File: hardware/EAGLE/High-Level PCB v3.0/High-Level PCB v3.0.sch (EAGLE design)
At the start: 57 parts, among them IC1 MCP2551, IC2 DS8921, IC3 DS8921, J1 Optical Mouse, J2 RaspπUart, J3 Gyro, J4 Micro-SD, J7 ODO_JACK, J8 DB9 Plug, J9 CAN Output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

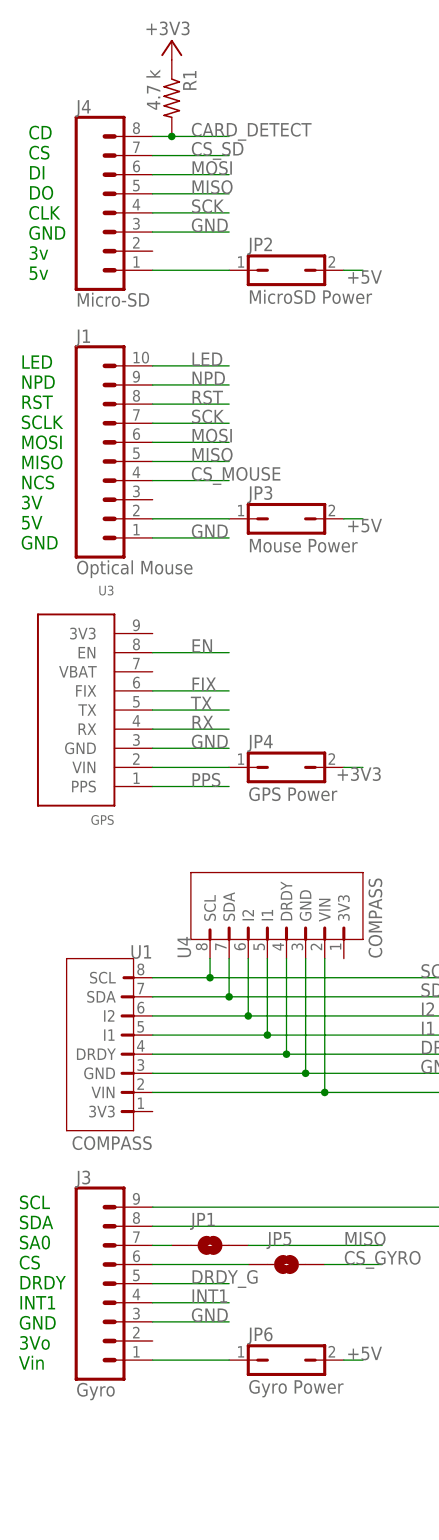
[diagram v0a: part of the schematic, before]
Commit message: added footprints
Includes footprints for all breakout boards except optical mouse
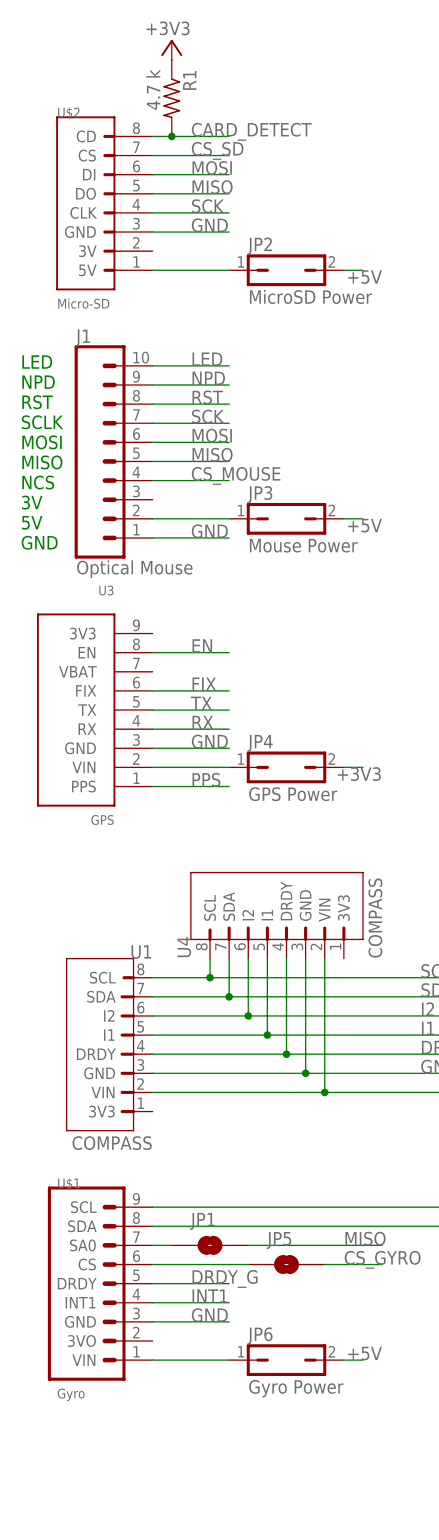
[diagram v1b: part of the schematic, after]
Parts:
- removed J3: Gyro, SparkFun-Connectors:CONN_09
- removed J4: Micro-SD, SparkFun-Connectors:CONN_08"
- added U$1: Gyro, ELCano_Footprints:ELGYRO_L3GD20H
- added U$2: Micro-SD, ELCano_Footprints:MINI_SD
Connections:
- net CARD_DETECT: now also U$2.CD; no longer J4.8
- net CS_SD: now also U$2.CS; no longer J4.7
- net DRDY_G: now also U$1.DRDY; no longer J3.5
- net GND: now also U$1.GND, U$2.GND; no longer J3.3, J4.3
- net INT1: now also U$1.INT1; no longer J3.4
- net MISO: now also U$2.DO; no longer J4.5
- net MOSI: now also U$2.DI; no longer J4.6
- net N$10: now also U$2.5V; no longer J4.1
- net N$19: now also U$1.CS; no longer J3.6
- net N$20: now also U$1.SA0; no longer J3.7
- net N$21: now also U$1.SDA; no longer J3.8
- net N$22: now also U$1.SCL; no longer J3.9
- net N$9: now also U$1.VIN; no longer J3.1
- net SCK: now also U$2.CLK; no longer J4.4
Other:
- note removed: "CD CS DI DO CLK GND 3v 5v"
- note removed: "SCL SDA SA0 CS DRDY INT1 GND 3Vo Vin"
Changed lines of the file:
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@@
 <part name="+3V31" library="supply1" library_urn="urn:adsk.eagle:library:371" deviceset="+3V3" device=""/>
 <part name="JP7" library="jumper" library_urn="urn:adsk.eagle:library:252" deviceset="JP1Q" device="" package3d_urn="urn:adsk.eagle:package:15455/1" value="Compass Power"/>
-<part name="J3" library="SparkFun-Connectors" library_urn="urn:adsk.eagle:library:513" deviceset="CONN_09" device="" package3d_urn="urn:adsk.eagle:package:38153/1" value="Gyro"/>
 <part name="JP6" library="jumper" library_urn="urn:adsk.eagle:library:252" deviceset="JP1Q" device="" package3d_urn="urn:adsk.eagle:package:15455/1" value="Gyro Power"/>
 <part name="JP1" library="SparkFun-Jumpers" deviceset="JUMPER-SMT_2_NO" device="_SILK" value=""/>
@@
 <part name="JP9" library="SparkFun-Jumpers" deviceset="JUMPER-SMT_3_1-NC_TRACE" device="_SILK" value=""/>
 <part name="GND5" library="SparkFun-PowerSymbols" deviceset="GND" device=""/>
-<part name="J4" library="SparkFun-Connectors" library_urn="urn:adsk.eagle:library:513" deviceset="CONN_08" device="&quot;" package3d_urn="urn:adsk.eagle:package:38138/1" value="Micro-SD"/>
 <part name="J1" library="SparkFun-Connectors" library_urn="urn:adsk.eagle:library:513" deviceset="CONN_10" device="&quot;" package3d_urn="urn:adsk.eagle:package:38157/1" value="Optical Mouse"/>
 <part name="TP1" library="testpad" library_urn="urn:adsk.eagle:library:385" deviceset="TP" device="PAD1-17" package3d_urn="urn:adsk.eagle:package:27949/1"/>
@@
 <part name="J2" library="tx_rxRasp" deviceset="CONN_02" device="" value="RaspπUart"/>
 <part name="GND14" library="SparkFun-PowerSymbols" deviceset="GND" device=""/>
+<part name="U$1" library="ELCano_Footprints" deviceset="ELGYRO_L3GD20H" device="" value="Gyro"/>
+<part name="U$2" library="ELCano_Footprints" deviceset="MINI_SD" device="" value="Micro-SD"/>
 </parts>
 <sheets>
@@
 5V
 GND</text>
-<text x="16.51" y="214.63" size="1.778" layer="91">CD
-CS
-DI
-DO
-CLK
-GND
-3v
-5v</text>
-<text x="15.24" y="69.85" size="1.778" layer="91">SCL
-SDA
-SA0
-CS
-DRDY
-INT1
-GND
-3Vo
-Vin</text>
 <text x="292.1" y="7.62" size="3.81" layer="97">The Elcano Project</text>
 </plain>
@@
 </instance>
 <instance part="JP7" gate="A" x="81.28" y="106.68" rot="R270"/>
-<instance part="J3" gate="G$1" x="22.86" y="81.28"/>
 <instance part="JP6" gate="A" x="50.8" y="71.12" rot="R270"/>
 <instance part="JP1" gate="G$1" x="40.64" y="86.36"/>
@@
 <instance part="JP9" gate="G$1" x="81.28" y="76.2" rot="MR180"/>
 <instance part="GND5" gate="1" x="175.26" y="33.02"/>
-<instance part="J4" gate="G$1" x="27.94" y="223.52"/>
 <instance part="J1" gate="G$1" x="22.86" y="198.12"/>
 <instance part="TP1" gate="G$1" x="360.68" y="76.2" smashed="yes" rot="R90">
@@
 <instance part="J2" gate="G$1" x="261.62" y="121.92" rot="MR0"/>
 <instance part="GND14" gate="1" x="254" y="114.3"/>
+<instance part="U$1" gate="G$1" x="20.32" y="68.58"/>
+<instance part="U$2" gate="G$1" x="20.32" y="213.36"/>
 </instances>
 <busses>
@@
 <wire x1="33.02" y1="231.14" x2="43.18" y2="231.14" width="0.1524" layer="91"/>
 <label x="38.1" y="231.14" size="1.778" layer="95"/>
-<pinref part="J4" gate="G$1" pin="7"/>
+<pinref part="U$2" gate="G$1" pin="CS"/>
 </segment>
 <segment>
@@
 <wire x1="33.02" y1="220.98" x2="43.18" y2="220.98" width="0.1524" layer="91"/>
 <label x="38.1" y="220.98" size="1.778" layer="95"/>
-<pinref part="J4" gate="G$1" pin="3"/>
-</segment>
-<segment>
-<pinref part="J3" gate="G$1" pin="3"/>
+<pinref part="U$2" gate="G$1" pin="GND"/>
+</segment>
+<segment>
 <wire x1="33.02" y1="76.2" x2="43.18" y2="76.2" width="0.1524" layer="91"/>
 <label x="38.1" y="76.2" size="1.778" layer="95"/>
+<pinref part="U$1" gate="G$1" pin="GND"/>
 </segment>
 <segment>
@@
 <net name="INT1" class="0">
 <segment>
-<pinref part="J3" gate="G$1" pin="4"/>
 <wire x1="33.02" y1="78.74" x2="43.18" y2="78.74" width="0.1524" layer="91"/>
 <label x="38.1" y="78.74" size="1.778" layer="95"/>
+<pinref part="U$1" gate="G$1" pin="INT1"/>
 </segment>
 <segment>
@@
 <net name="DRDY_G" class="0">
 <segment>
-<pinref part="J3" gate="G$1" pin="5"/>
 <wire x1="33.02" y1="81.28" x2="43.18" y2="81.28" width="0.1524" layer="91"/>
 <label x="38.1" y="81.28" size="1.778" layer="95"/>
+<pinref part="U$1" gate="G$1" pin="DRDY"/>
 </segment>
 <segment>
@@
 <wire x1="33.02" y1="223.52" x2="43.18" y2="223.52" width="0.1524" layer="91"/>
 <label x="38.1" y="223.52" size="1.778" layer="95"/>
-<pinref part="J4" gate="G$1" pin="4"/>
+<pinref part="U$2" gate="G$1" pin="CLK"/>
 </segment>
 <segment>
@@
 <wire x1="33.02" y1="228.6" x2="43.18" y2="228.6" width="0.1524" layer="91"/>
 <label x="38.1" y="228.6" size="1.778" layer="95"/>
-<pinref part="J4" gate="G$1" pin="6"/>
+<pinref part="U$2" gate="G$1" pin="DI"/>
 </segment>
 <segment>
@@
 <wire x1="33.02" y1="226.06" x2="43.18" y2="226.06" width="0.1524" layer="91"/>
 <label x="38.1" y="226.06" size="1.778" layer="95"/>
-<pinref part="J4" gate="G$1" pin="5"/>
+<pinref part="U$2" gate="G$1" pin="DO"/>
 </segment>
 <segment>
@@
 <segment>
 <wire x1="43.18" y1="71.12" x2="33.02" y2="71.12" width="0.1524" layer="91"/>
-<pinref part="J3" gate="G$1" pin="1"/>
 <pinref part="JP6" gate="A" pin="1"/>
+<pinref part="U$1" gate="G$1" pin="VIN"/>
 </segment>
 </net>
@@
 <pinref part="JP2" gate="A" pin="1"/>
 <wire x1="33.02" y1="215.9" x2="43.18" y2="215.9" width="0.1524" layer="91"/>
-<pinref part="J4" gate="G$1" pin="1"/>
+<pinref part="U$2" gate="G$1" pin="5V"/>
 </segment>
 </net>
@@
 <junction x="35.56" y="233.68"/>
 <label x="38.1" y="233.68" size="1.778" layer="95"/>
-<pinref part="J4" gate="G$1" pin="8"/>
+<pinref part="U$2" gate="G$1" pin="CD"/>
 </segment>
 <segment>
@@
 <net name="N$19" class="0">
 <segment>
-<pinref part="J3" gate="G$1" pin="6"/>
 <pinref part="JP5" gate="G$1" pin="1"/>
 <wire x1="33.02" y1="83.82" x2="45.72" y2="83.82" width="0.1524" layer="91"/>
+<pinref part="U$1" gate="G$1" pin="CS"/>
 </segment>
 </net>
 <net name="N$20" class="0">
 <segment>
-<pinref part="J3" gate="G$1" pin="7"/>
 <pinref part="JP1" gate="G$1" pin="1"/>
 <wire x1="33.02" y1="86.36" x2="35.56" y2="86.36" width="0.1524" layer="91"/>
+<pinref part="U$1" gate="G$1" pin="SA0"/>
 </segment>
 </net>
 <net name="N$22" class="0">
 <segment>
-<pinref part="J3" gate="G$1" pin="9"/>
 <wire x1="33.02" y1="91.44" x2="76.2" y2="91.44" width="0.1524" layer="91"/>
 <pinref part="JP8" gate="G$1" pin="2"/>
+<pinref part="U$1" gate="G$1" pin="SCL"/>
 </segment>
 </net>
 <net name="N$21" class="0">
 <segment>
-<pinref part="J3" gate="G$1" pin="8"/>
 <wire x1="33.02" y1="88.9" x2="73.66" y2="88.9" width="0.1524" layer="91"/>
 <wire x1="73.66" y1="88.9" x2="73.66" y2="76.2" width="0.1524" layer="91"/>
 <wire x1="73.66" y1="76.2" x2="76.2" y2="76.2" width="0.1524" layer="91"/>
 <pinref part="JP9" gate="G$1" pin="2"/>
-</segment>
-</net>
+<pinref part="U$1" gate="G$1" pin="SDA"/>
+</segment>
+</net>

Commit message: Used larger resistor footprints
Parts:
- R1, R4, R5, R6: device resistor:R-US_0204/5 -> resistor:R-US_0204/7
- R2, R3, R7, R8: device rcl:R-US_0204/5 -> rcl:R-US_0204/7
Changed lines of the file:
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@@
 <part name="J7" library="elcanoParts" deviceset="ODO_JACK" device=""/>
 <part name="C2" library="capacitor-wima" library_urn="urn:adsk.eagle:library:116" deviceset="C" device="2.5/5" package3d_urn="urn:adsk.eagle:package:5407/1" value="1 uF"/>
-<part name="R4" library="resistor" library_urn="urn:adsk.eagle:library:348" deviceset="R-US_" device="0204/5" package3d_urn="urn:adsk.eagle:package:25955/1" value="4.7 k"/>
+<part name="R4" library="resistor" library_urn="urn:adsk.eagle:library:348" deviceset="R-US_" device="0204/7" package3d_urn="urn:adsk.eagle:package:25945/1" value="4.7 k"/>
 <part name="GND3" library="SparkFun-PowerSymbols" deviceset="GND" device=""/>
 <part name="X1" library="con-subd" library_urn="urn:adsk.eagle:library:189" deviceset="M25" device="H" package3d_urn="urn:adsk.eagle:package:10312/1" value="Vehicle control"/>
@@
 <part name="S2" library="elcanoParts" deviceset="DPDT_DEV" device="6X5MM_PAC" value="SPI Direction"/>
 <part name="X2" library="con-kycon" library_urn="urn:adsk.eagle:library:157" deviceset="GLX-S-88M" device="" package3d_urn="urn:adsk.eagle:package:7680/1" value="RJ45"/>
-<part name="R7" library="rcl" library_urn="urn:adsk.eagle:library:334" deviceset="R-US_" device="0204/5" package3d_urn="urn:adsk.eagle:package:23488/1" value="100"/>
+<part name="R7" library="rcl" library_urn="urn:adsk.eagle:library:334" deviceset="R-US_" device="0204/7" package3d_urn="urn:adsk.eagle:package:23498/1" value="100"/>
 <part name="X3" library="con-kycon" library_urn="urn:adsk.eagle:library:157" deviceset="GLX-S-88M" device="" package3d_urn="urn:adsk.eagle:package:7680/1" value="RJ45"/>
-<part name="R8" library="rcl" library_urn="urn:adsk.eagle:library:334" deviceset="R-US_" device="0204/5" package3d_urn="urn:adsk.eagle:package:23488/1" value="100"/>
+<part name="R8" library="rcl" library_urn="urn:adsk.eagle:library:334" deviceset="R-US_" device="0204/7" package3d_urn="urn:adsk.eagle:package:23498/1" value="100"/>
 <part name="C3" library="capacitor-wima" library_urn="urn:adsk.eagle:library:116" deviceset="C" device="2.5/5" package3d_urn="urn:adsk.eagle:package:5407/1" value="0.1 uF"/>
 <part name="C4" library="capacitor-wima" library_urn="urn:adsk.eagle:library:116" deviceset="C" device="2.5/5" package3d_urn="urn:adsk.eagle:package:5407/1" value="0.1 uF"/>
@@
 <part name="JP3" library="jumper" library_urn="urn:adsk.eagle:library:252" deviceset="JP1Q" device="" package3d_urn="urn:adsk.eagle:package:15455/1" value="Mouse Power"/>
 <part name="JP4" library="jumper" library_urn="urn:adsk.eagle:library:252" deviceset="JP1Q" device="" package3d_urn="urn:adsk.eagle:package:15455/1" value="GPS Power"/>
-<part name="R6" library="resistor" library_urn="urn:adsk.eagle:library:348" deviceset="R-US_" device="0204/5" package3d_urn="urn:adsk.eagle:package:25955/1" value="4.7 k"/>
-<part name="R5" library="resistor" library_urn="urn:adsk.eagle:library:348" deviceset="R-US_" device="0204/5" package3d_urn="urn:adsk.eagle:package:25955/1" value="4.7 k"/>
+<part name="R6" library="resistor" library_urn="urn:adsk.eagle:library:348" deviceset="R-US_" device="0204/7" package3d_urn="urn:adsk.eagle:package:25945/1" value="4.7 k"/>
+<part name="R5" library="resistor" library_urn="urn:adsk.eagle:library:348" deviceset="R-US_" device="0204/7" package3d_urn="urn:adsk.eagle:package:25945/1" value="4.7 k"/>
 <part name="IC1" library="ic-package" library_urn="urn:adsk.eagle:library:239" deviceset="DIL8" device="" package3d_urn="urn:adsk.eagle:package:14440/1" value="MCP2551"/>
-<part name="R3" library="rcl" library_urn="urn:adsk.eagle:library:334" deviceset="R-US_" device="0204/5" package3d_urn="urn:adsk.eagle:package:23488/1" value="120"/>
-<part name="R2" library="rcl" library_urn="urn:adsk.eagle:library:334" deviceset="R-US_" device="0204/5" package3d_urn="urn:adsk.eagle:package:23488/1" value="10 k"/>
+<part name="R3" library="rcl" library_urn="urn:adsk.eagle:library:334" deviceset="R-US_" device="0204/7" package3d_urn="urn:adsk.eagle:package:23498/1" value="120"/>
+<part name="R2" library="rcl" library_urn="urn:adsk.eagle:library:334" deviceset="R-US_" device="0204/7" package3d_urn="urn:adsk.eagle:package:23498/1" value="10 k"/>
 <part name="P+1" library="supply1" library_urn="urn:adsk.eagle:library:371" deviceset="+5V" device=""/>
 <part name="GND1" library="SparkFun-PowerSymbols" deviceset="GND" device=""/>
@@
 <part name="+3V35" library="supply1" library_urn="urn:adsk.eagle:library:371" deviceset="+3V3" device=""/>
 <part name="GND7" library="SparkFun-PowerSymbols" deviceset="GND" device=""/>
-<part name="R1" library="resistor" library_urn="urn:adsk.eagle:library:348" deviceset="R-US_" device="0204/5" package3d_urn="urn:adsk.eagle:package:25955/1" value="4.7 k"/>
+<part name="R1" library="resistor" library_urn="urn:adsk.eagle:library:348" deviceset="R-US_" device="0204/7" package3d_urn="urn:adsk.eagle:package:25945/1" value="4.7 k"/>
 <part name="+3V31" library="supply1" library_urn="urn:adsk.eagle:library:371" deviceset="+3V3" device=""/>
 <part name="JP7" library="jumper" library_urn="urn:adsk.eagle:library:252" deviceset="JP1Q" device="" package3d_urn="urn:adsk.eagle:package:15455/1" value="Compass Power"/>
